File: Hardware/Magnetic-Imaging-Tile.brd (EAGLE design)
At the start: 52.1 x 34.3 mm, 101 parts, among them U01 DRV5053, U02 DRV5053, U03 DRV5053, U04 DRV5053, U05 DRV5053, U06 DRV5053, U07 DRV5053, U08 CD74HC4067, U09 DRV5053, U10 DRV5053, U104 SN74HC590A, U105 SN74LVC1G139, U106 AD7680, U11 DRV5053, U12 DRV5053, U13 DRV5053, U14 DRV5053, U15 DRV5053, U16 DRV5053, U17 DRV5053, U18 CD74HC4067, U19 CD74HC4067, U20 DRV5053, U21 DRV5053, U22 DRV5053, U23 DRV5053, U24 DRV5053, U25 DRV5053, U26 DRV5053, U27 DRV5053, U28 CD74HC4067, U30 DRV5053, U31 DRV5053, U32 DRV5053, U33 DRV5053, U34 DRV5053, U35 DRV5053, U36 DRV5053, U37 DRV5053, U40 DRV5053, U41 DRV5053, U42 DRV5053, U43 DRV5053, U44 DRV5053, U45 DRV5053, U46 DRV5053, U47 DRV5053, U50 DRV5053, U51 DRV5053, U52 DRV5053, U53 DRV5053, U54 DRV5053, U55 DRV5053, U56 DRV5053, U57 DRV5053, U60 DRV5053, U61 DRV5053, U62 DRV5053, U63 DRV5053, U64 DRV5053, U65 DRV5053, U66 DRV5053, U67 DRV5053, U70 DRV5053, U71 DRV5053, U72 DRV5053, U73 DRV5053, U74 DRV5053, U75 DRV5053, U76 DRV5053, U77 DRV5053

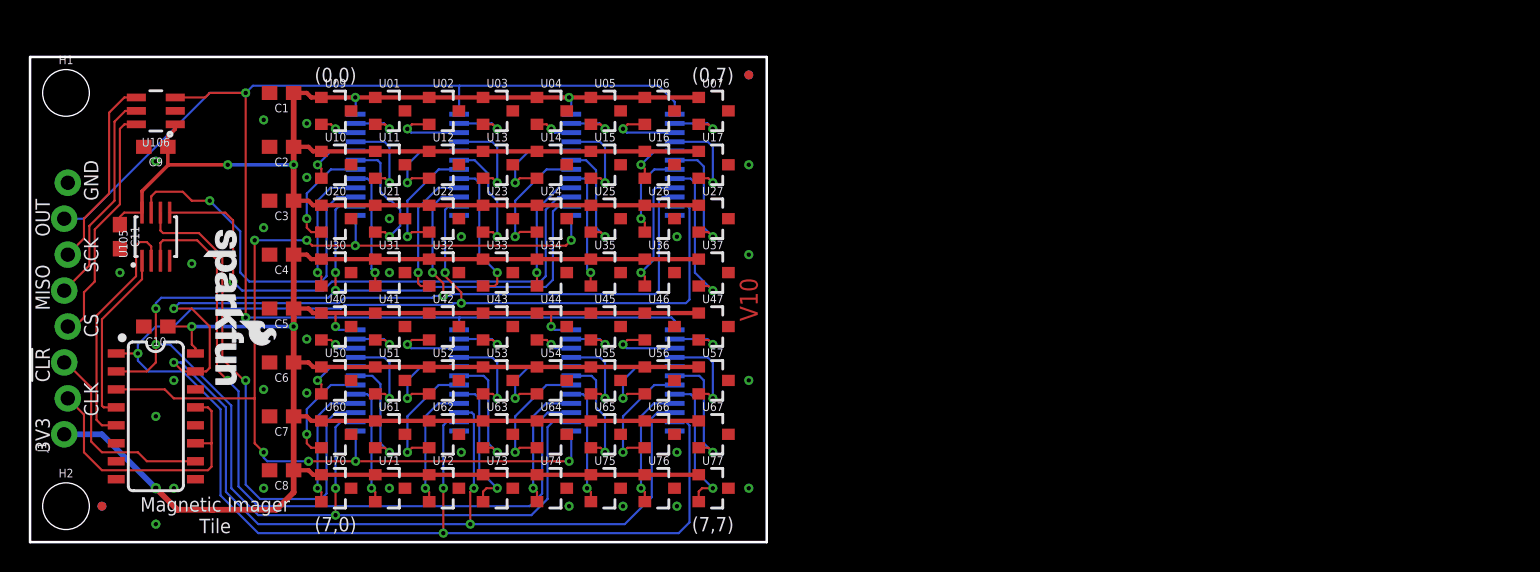
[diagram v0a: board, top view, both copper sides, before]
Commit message: Update
-Changes silk to vector
-Added order instructions
-Updated Design By
-OSH and SPARKFUN added to sch and board as part
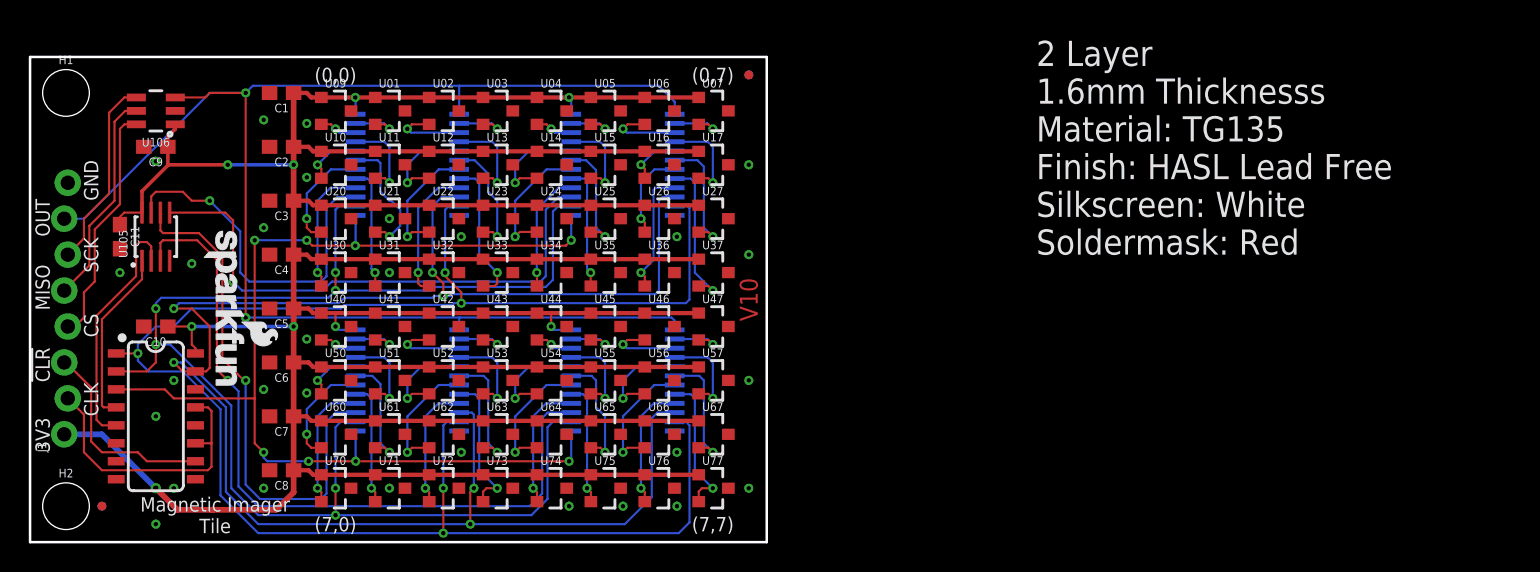
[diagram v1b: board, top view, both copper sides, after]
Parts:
- removed LOGO2: OSHW-LOGOS, SparkFun-Aesthetics:OSHW-LOGO-S
- added LOGO3: SFE_LOGO_NAME.1_INCH, SparkFun-Aesthetics:SFE_LOGO_NAME_.1
- added LOGO4: OSHW-LOGOS, SparkFun-Aesthetics:OSHW-LOGO-S
- added U$2: (no value), SparkFun-Aesthetics:SFE_LOGO_FLAME_.1
- LOGO1: value SFE_LOGO_NAME_FLAME.1_INCH -> SPECIAL_INSTRUCTIONS-ORDERING; device SparkFun-Aesthetics:SFE_LOGO_NAME_FLAME_.1 -> SparkFun-Aesthetics:ORDERING_INSTRUCTIONS
- moved LOGO1 61.2 mm to (66.0, 48.3), turned to 0 degrees
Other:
- board text added: "2 Layer 1.6mm Thicknesss Material: TG135 Finish: HASL Lead Free Silkscreen: White Soldermask: Red"
- board text added: "Peter Jansen Revised by: Chris Bryant"
- board text removed: "Peter Jansen"
